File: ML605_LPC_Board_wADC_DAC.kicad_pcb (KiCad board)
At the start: 4 copper layers, 100 x 100 mm, 112 parts, among them IC1 ADC10D040CIVS_NOPB, IC2 AD8137YRZ-REEL, IC3 AD8137YRZ-REEL, IC4 DAC5652IPFB, J1 ASP-134604-01, J10 Conn_02x06_Odd_Even, J11 Conn_02x06_Odd_Even, J12 Conn_02x06_Odd_Even, J13 Conn_01x03_Pin, J14 Conn_01x03_Pin, J2 Conn_01x03_Pin, J3 Conn_01x03_Pin, J4 SMA Connector, J5 SMA Connector, J6 Conn_01x03_Pin, J7 Conn_01x03_Pin, J8 SMA Connector, J9 SMA Connector, U1 LMV7219M7, U2 LMV7219M7, U3 NCV317, U4 LMH6702MA, U5 LMH6702MA

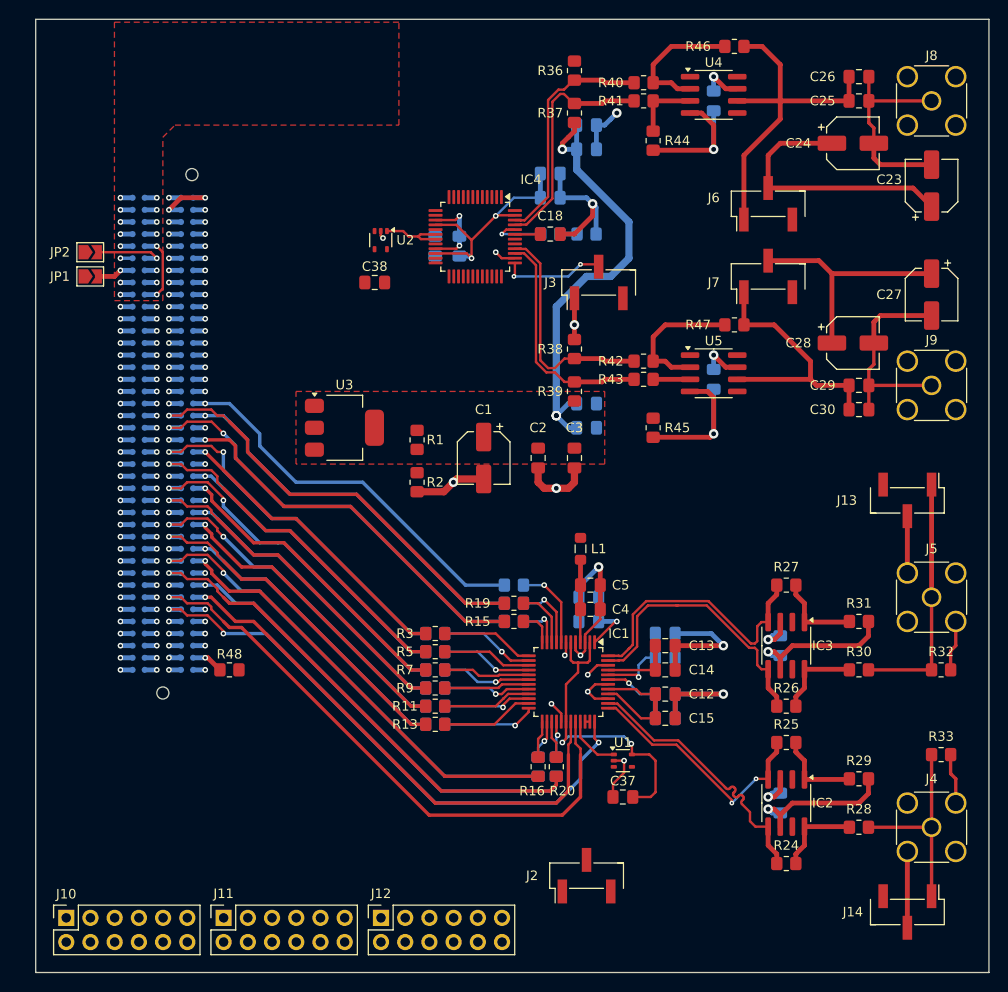
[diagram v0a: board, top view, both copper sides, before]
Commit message: Second commit, routed digital data inputs of DAC
Now I have problems routing the WRTA & WRTB pins of the DAC. Will probably have to reassign some pins of the digital data inputs (potential solution: I could make the WRTA/WRTB pair be situated at LA29, and the DAC_DB input pins would have to be cascaded down. DAC_DB1/DAC_DB0 would then have to be moved to the other side of the LPC connector, probably where WRTA/WRTB are now, at LA26). It'll look weird in the pinout diagram, but at least it'll work (hopefully :@    )
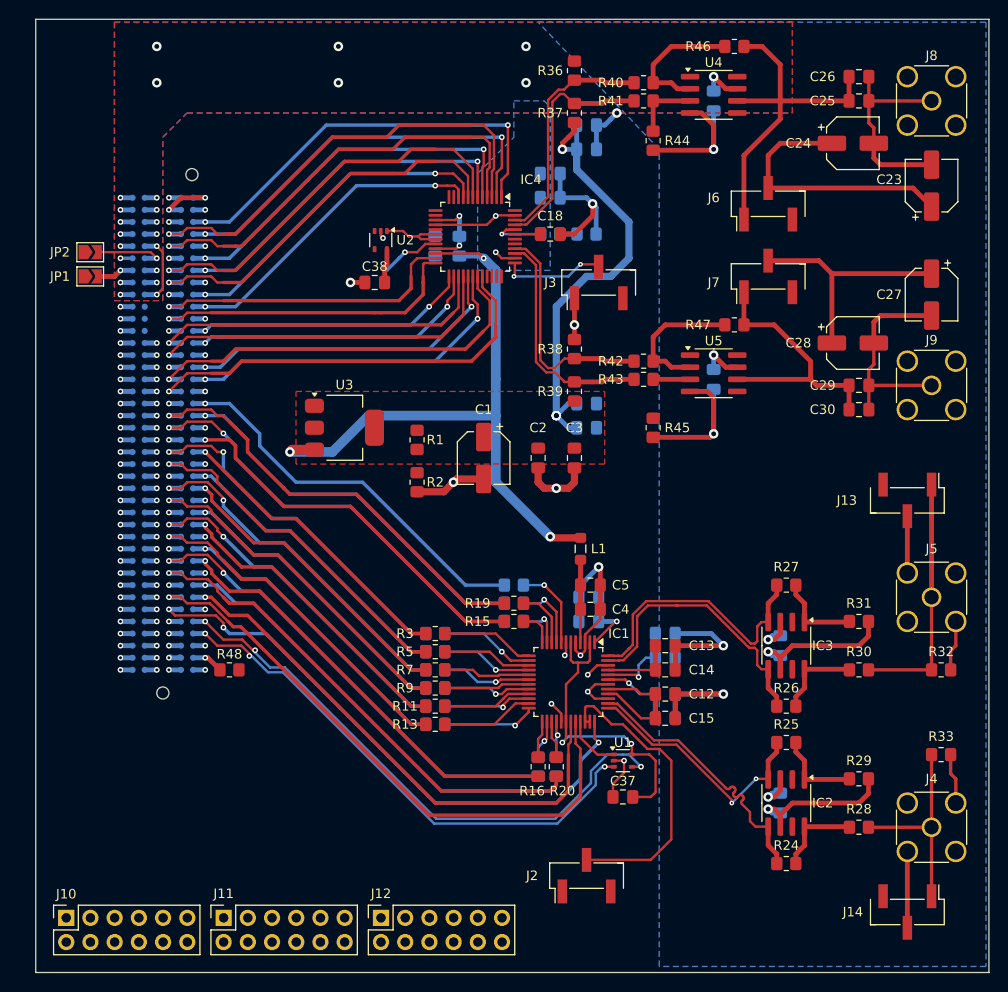
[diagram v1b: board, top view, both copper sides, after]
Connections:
- IC4 pad 1: /LA28_P -> /LA32_N
- IC4 pad 10: /LA32_N -> /LA28_P
- IC4 pad 17: /LA01_P_CC -> /LA26_N
- IC4 pad 2: /LA28_N -> /LA32_P
- IC4 pad 20: /LA01_N_CC -> /LA26_P
- IC4 pad 3: /LA31_P -> /LA33_N
- IC4 pad 4: /LA31_N -> /LA33_P
- IC4 pad 5: /LA30_P -> /LA30_N
- IC4 pad 6: /LA30_N -> /LA30_P
- IC4 pad 7: /LA33_P -> /LA31_N
- IC4 pad 8: /LA33_N -> /LA31_P
- IC4 pad 9: /LA32_P -> /LA28_N
- J10 pad 1: /LA06_P -> /LA01_P_CC
- J10 pad 2: /LA09_P -> /LA05_P
- J10 pad 3: /LA06_N -> /LA01_N_CC
- J10 pad 4: /LA09_N -> /LA05_N
- J10 pad 5: /LA05_P -> /LA06_P
- J10 pad 6: /LA10_P -> /LA09_P
- J10 pad 7: /LA05_N -> /LA06_N
- J10 pad 8: /LA10_N -> /LA09_N
- J11 pad 1: /LA13_P -> /LA10_P
- J11 pad 2: /LA17_P_CC -> /LA14_P
- J11 pad 3: /LA13_N -> /LA10_N
- J11 pad 4: /LA17_N_CC -> /LA14_N
- J11 pad 5: /LA14_P -> /LA13_P
- J11 pad 6: /LA18_P_CC -> /LA17_P_CC
- J11 pad 7: /LA14_N -> /LA13_N
- J11 pad 8: /LA18_N_CC -> /LA17_N_CC
- J12 pad 1: /LA23_P -> /LA18_P_CC
- J12 pad 3: /LA23_N -> /LA18_N_CC
- J12 pad 5: /LA26_P -> /LA23_P
- J12 pad 7: /LA26_N -> /LA23_N
- U1 pad 3: /CLK1_M2C_P -> /CLK0_M2C_P
- U1 pad 4: /CLK1_M2C_N -> /CLK0_M2C_N
- U2 pad 3: /CLK0_M2C_P -> /CLK1_M2C_P
- U2 pad 4: /CLK0_M2C_N -> /CLK1_M2C_N
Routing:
- net /CLK0_M2C_N: track 1.27 -> 60.7 mm, vias 1 -> 3
- net /CLK0_M2C_P: track 1.27 -> 55.8 mm, vias 1 -> 3
- net 3V3: track 67.7 -> 120.1 mm, vias 11 -> 19
- net /LA33_N: track 1.03 -> 47.4 mm
- net /LA33_P: track 1.03 -> 46.0 mm
- net /LA32_N: track 1.27 -> 45.1 mm, vias 1 -> 2
- net /LA22_P: track 1.03 -> 44.6 mm
- net /LA32_P: track 1.27 -> 43.1 mm, vias 1 -> 2
- net /LA22_N: track 1.03 -> 42.7 mm
- net /LA31_N: track 1.03 -> 42.5 mm
- net /LA31_P: track 1.03 -> 41.0 mm
- net /LA30_N: track 1.27 -> 40.3 mm, vias 1 -> 2
- net /LA30_P: track 1.27 -> 38.3 mm, vias 1 -> 2
- net /LA25_P: track 1.03 -> 37.7 mm
- net /LA21_P: track 1.27 -> 37.1 mm, vias 1 -> 2
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- added copper zone on B.Cu, net 3V3

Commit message: The ADC/DAC part of the board is done
Now I just need to figure out how to do the GPIO breakout, but I have a lot more flexibility here. Ideally, I'd like to keep the PMOD connector format, however I'm not sure if that is going to be possible. If I can't do that due to routing issues, than I can probably just stick a 50-something pin header on the the top side of the board at the left edge, on the other side of the LPC connector and call it a day.
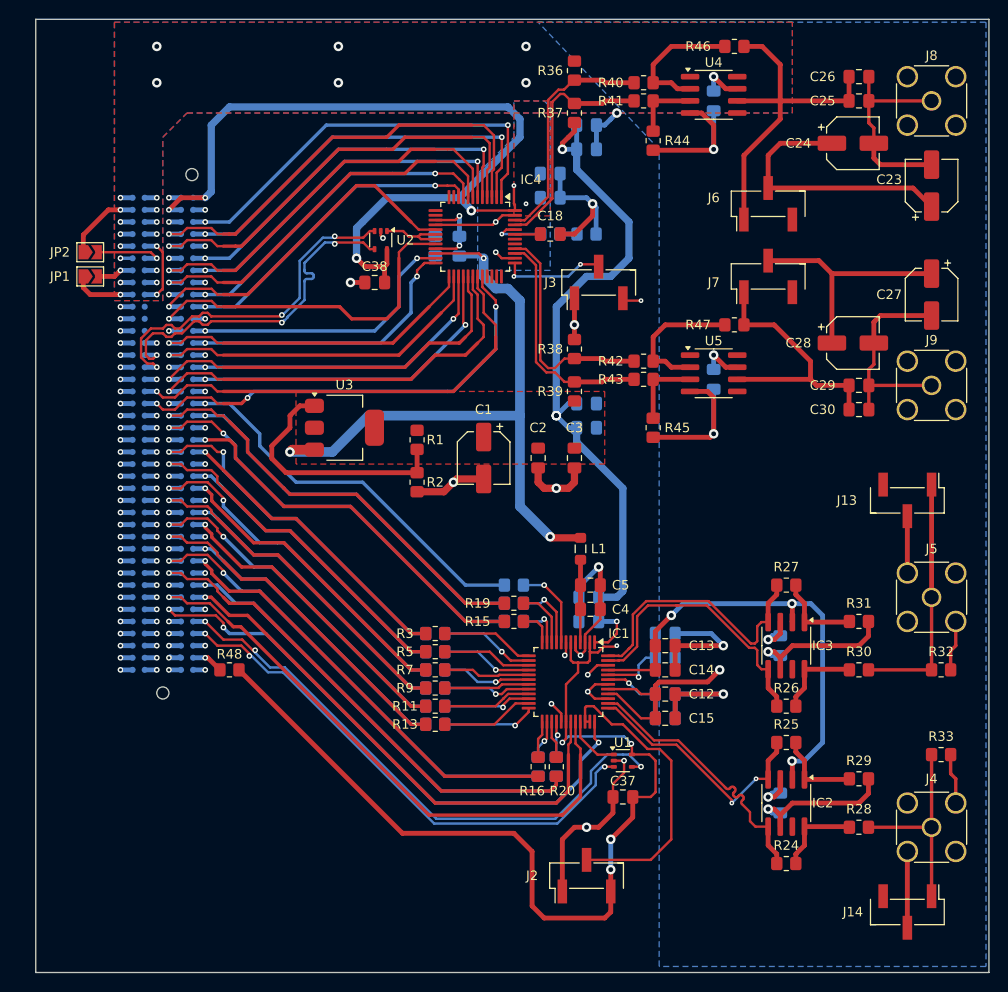
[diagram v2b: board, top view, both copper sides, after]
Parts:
- removed J10, J11, J12: Conn_02x06_Odd_Even, Connector_PinSocket_2.54mm:PinSocket_2x06_P2.54mm_Vertical
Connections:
- IC4 pad 17: /LA26_N -> /LA29_N
- IC4 pad 20: /LA26_P -> /LA29_P
- IC4 pad 23: /LA29_N -> /LA24_N
- IC4 pad 24: /LA29_P -> /LA24_P
- IC4 pad 25: /LA24_N -> /LA25_N
- IC4 pad 26: /LA24_P -> /LA25_P
- IC4 pad 27: /LA25_N -> /LA21_N
- IC4 pad 28: /LA25_P -> /LA21_P
- IC4 pad 29: /LA21_N -> /LA22_N
- IC4 pad 30: /LA21_P -> /LA22_P
- IC4 pad 31: /LA22_N -> /LA23_N
- IC4 pad 32: /LA22_P -> /LA23_P
- U2 pad 3: /CLK1_M2C_P -> /LA26_P
- U2 pad 4: /CLK1_M2C_N -> /LA26_N
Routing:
- net VADJ: track 42.9 -> 255.6 mm, vias 4 -> 11
- net /LA23_P: track 1.03 -> 48.2 mm, vias 1 -> 3
- net /LA23_N: track 1.03 -> 47.9 mm
- net /ADC_Circuit/VCM_ADC: track 7.51 -> 49.6 mm, vias 0 -> 3
- net /LA26_N: track 1.03 -> 37.3 mm, vias 1 -> 3
- net /LA26_P: track 7.29 -> 37.3 mm, vias 2 -> 3
- net Net-(U3-ADJ): track 0.00 -> 26.6 mm
- net 1V5: track 55.2 -> 77.9 mm
- net GNDA: track 278.7 -> 297.7 mm, vias 84 -> 85
- net 3V3: track 120.1 -> 138.5 mm, vias 19 -> 21
- net /LA29_N: track 32.6 -> 36.8 mm
- net Net-(U5-+): track 3.88 -> 7.95 mm
- net /LA29_P: track 33.3 -> 37.2 mm
- net /LA25_N: track 36.2 -> 34.5 mm
- net /LA22_N: track 42.7 -> 41.3 mm
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
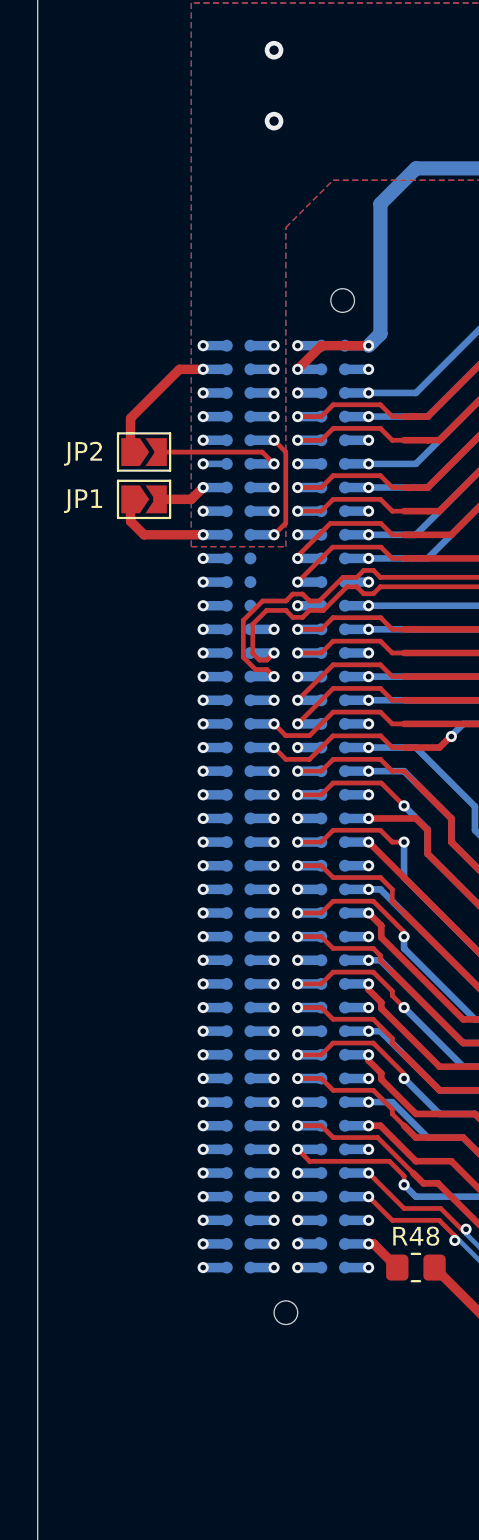
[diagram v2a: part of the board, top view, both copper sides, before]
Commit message: Routing is done
Routing is finally done! Now I just need to add some silkscreen markings, maybe a label, order number placement, and I need to place some ground stitching vias here and there
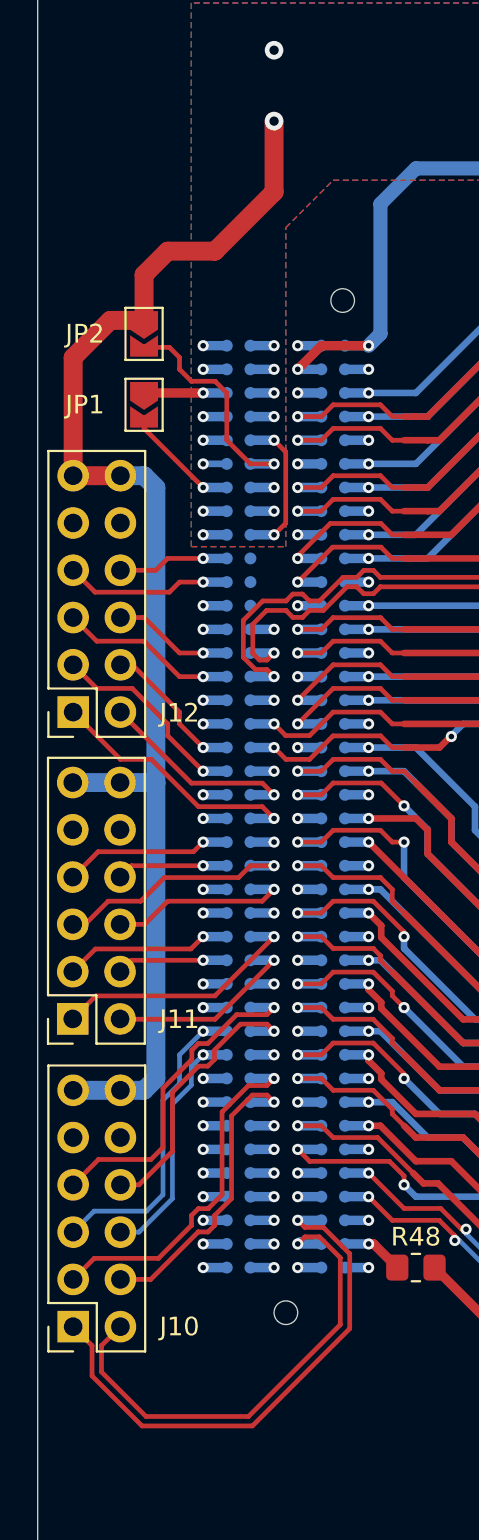
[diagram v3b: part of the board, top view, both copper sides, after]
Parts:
- added J10: Conn_02x06_Odd_Even, Connector_PinSocket_2.54mm:PinSocket_2x06_P2.54mm_Vertical, F.Cu at (76.9, 121.4)
- added J11: Conn_02x06_Odd_Even, Connector_PinSocket_2.54mm:PinSocket_2x06_P2.54mm_Vertical, F.Cu at (76.9, 104.9)
- added J12: Conn_02x06_Odd_Even, Connector_PinSocket_2.54mm:PinSocket_2x06_P2.54mm_Vertical, F.Cu at (76.9, 88.4)
- moved JP2 6.35 mm to (80.7, 68.1), turned to -90 degrees
- moved JP1 5.08 mm to (80.7, 71.9), turned to -90 degrees
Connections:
- J1 pad D8: /LA01_P_CC -> /LA01_P
- J1 pad D9: /LA01_N_CC -> /LA01_N
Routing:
- net 3V3: track 138.5 -> 203.4 mm
- net /CLK1_M2C_N: track 1.03 -> 28.8 mm
- net /CLK1_M2C_P: track 1.37 -> 26.6 mm
- net /LA01_N: track 0.00 -> 19.2 mm, vias 0 -> 1
- net /LA05_N: track 1.03 -> 17.9 mm
- net /LA01_P: track 0.00 -> 16.5 mm, vias 0 -> 1
- net /LA06_N: track 1.03 -> 16.4 mm
- net /LA05_P: track 1.03 -> 15.2 mm
- net /LA17_P_CC: track 1.03 -> 14.2 mm
- net /LA09_N: track 1.03 -> 13.7 mm
- net /LA13_N: track 1.03 -> 13.2 mm
- net /LA06_P: track 1.03 -> 13.0 mm
- net /LA17_N_CC: track 1.03 -> 11.1 mm
- net /LA18_P_CC: track 1.03 -> 10.8 mm
- net /LA09_P: track 1.03 -> 10.6 mm
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
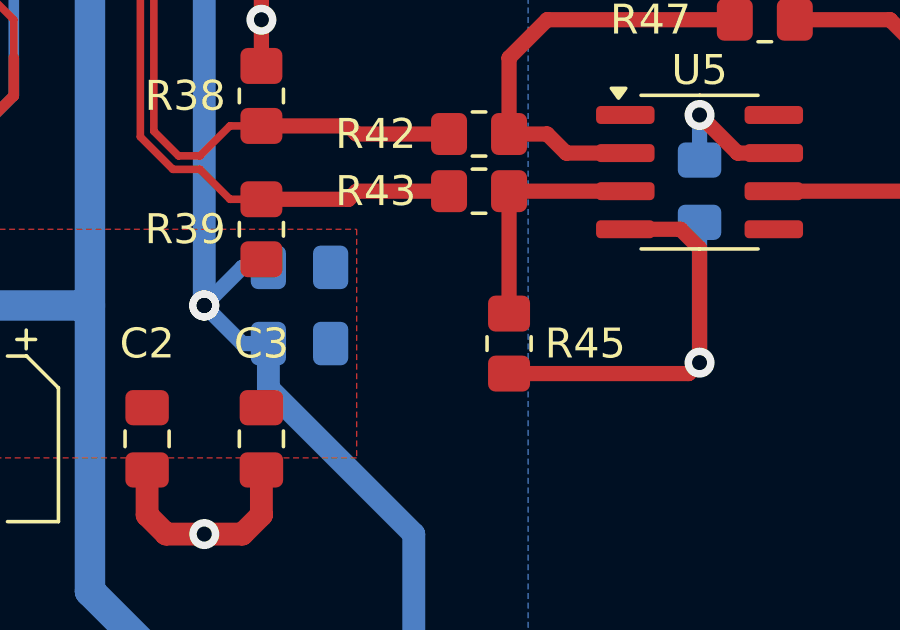
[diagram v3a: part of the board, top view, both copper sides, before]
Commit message: Minor tracing mistakes fixed
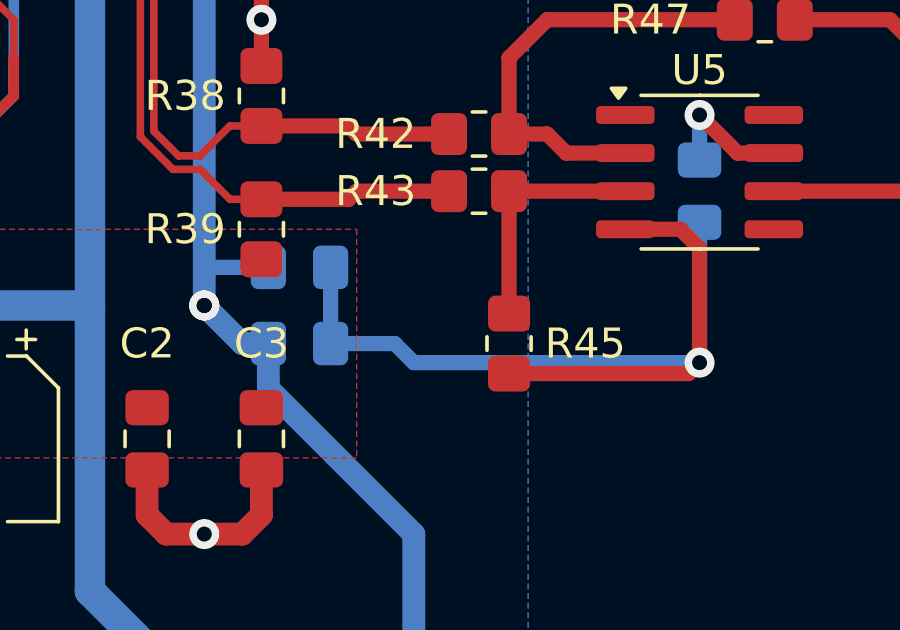
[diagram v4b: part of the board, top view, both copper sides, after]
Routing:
- net GNDA: track 295.5 -> 310.6 mm
- net 1V5: track 77.9 -> 77.4 mm
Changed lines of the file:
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@@
+	)
+	(segment
+		(start 146.12 93.485)
+		(end 136.595 93.485)
+		(width 0.508)
+		(layer "B.Cu")
+		(net 1)
 	)
 	(segment
@@
 	)
 	(segment
+		(start 136.595 93.485)
+		(end 135.96 92.85)
+		(width 0.508)
+		(layer "B.Cu")
+		(net 1)
+	)
+	(segment
 		(start 142.0775 114.44)
 		(end 142.0775 116.98)
@@
 	)
 	(segment
+		(start 133.8225 92.85)
+		(end 133.8225 90.31)
+		(width 0.508)
+		(layer "B.Cu")
+		(net 1)
+	)
+	(segment
 		(start 86.549 111.9)
 		(end 87.581 111.9)
@@
 		(start 147.136 115.71)
 		(end 145.866 114.44)
+		(width 0.508)
+		(layer "B.Cu")
+		(net 1)
+	)
+	(segment
+		(start 135.96 92.85)
+		(end 133.8225 92.85)
 		(width 0.508)
 		(layer "B.Cu")
@@
 	)
 	(segment
-		(start 131.7475 90.31)
-		(end 130.88 90.31)
-		(width 0.508)
-		(layer "B.Cu")
-		(net 2)
-	)
-	(segment
 		(start 135.325 76.975)
 		(end 137.23 75.07)
@@
 		(start 131.7475 92.85)
 		(end 130.88 92.85)
-		(width 0.508)
+		(width 0.762)
 		(layer "B.Cu")
 		(net 2)
@@
 	)
 	(segment
-		(start 130.88 90.31)
-		(end 129.61 91.58)
-		(width 0.508)
-		(layer "B.Cu")
-		(net 2)
-	)
-	(segment
 		(start 137.23 75.07)
 		(end 137.23 71.26)
@@
 	)
 	(segment
+		(start 131.7475 90.31)
+		(end 129.61 90.31)
+		(width 0.508)
+		(layer "B.Cu")
+		(net 2)
+	)
+	(segment
 		(start 129.61 80.15)
 		(end 132.785 76.975)
@@
 		(start 130.88 92.85)
 		(end 129.61 91.58)
-		(width 0.508)
-		(layer "B.Cu")
-		(net 2)
+		(width 0.762)
+		(layer "B.Cu")
+		(net 2)
